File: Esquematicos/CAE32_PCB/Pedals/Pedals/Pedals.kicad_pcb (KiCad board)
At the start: 4 copper layers, 94.9 x 76.5 mm, 105 parts, among them J1 SPI_MASTER, J10 Conn_01x03_Female, J11 Conn_01x03_Female, J12 Conn_01x03_Female, J13 Conn_01x03_Female, J14 Conn_01x03_Female, J15 USB_C_Receptacle, J16 UART_PGR, J17 ST-Link, J18 LC_2, J19 LC_1, J2 CAN, J20 LC_3, J3 PGRM and SPI, J4 Conn_01x03_Female, J5 Conn_01x03_Female, J6 Conn_01x03_Female, J7 Conn_01x03_Female, J8 Conn_01x03_Female, J9 Conn_01x03_Female, Q1 MMBT3906, Q2 MMBT3906, Q3 MMBT3906, SW1 CONFIG, SW2 BOOT, SW3 RST, U1 STM32F072RBTx, U2 REF3033, U3 ADC128S102, U4 LDL1117, U5 HX711, U6 HX711, U7 HX711

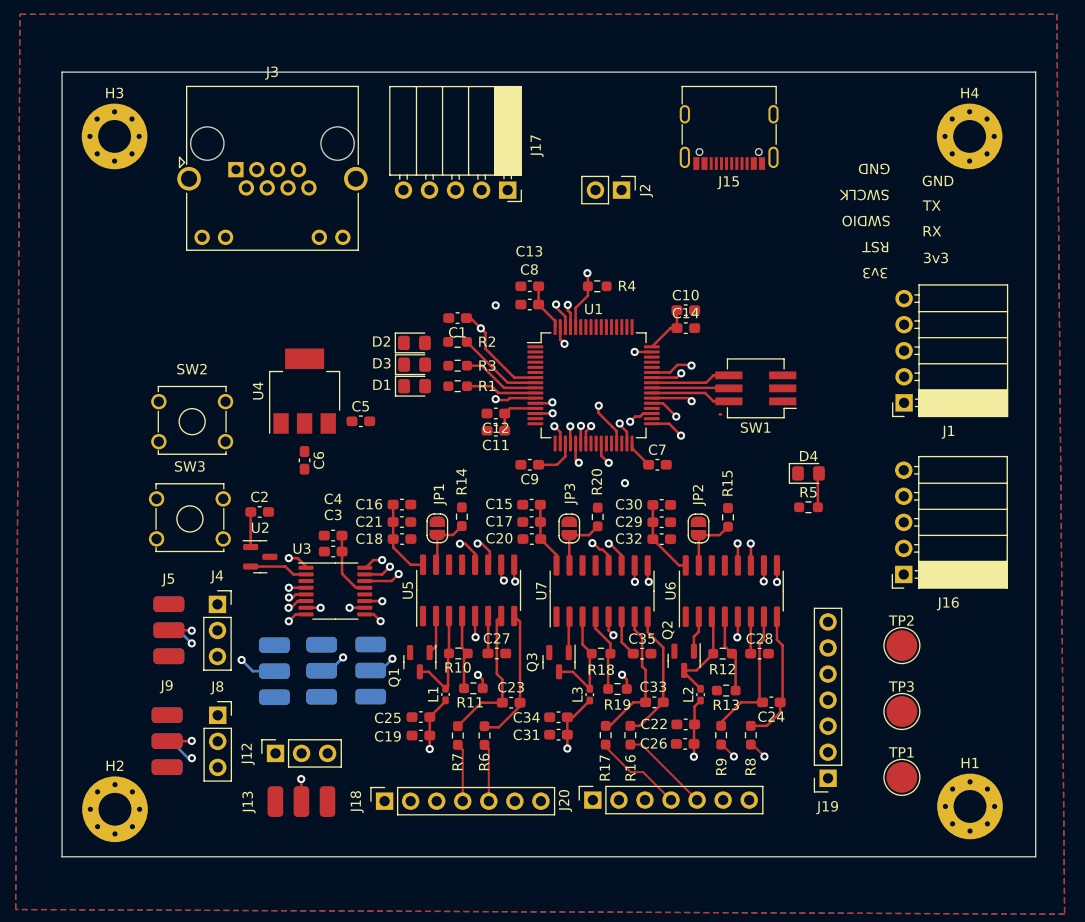
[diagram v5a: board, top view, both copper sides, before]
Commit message: Update: esquematicos de PCB, reorganizando elementos para hacer mas compacta la pcb, ademas de agregar serigrafia e imagenes de la PCB
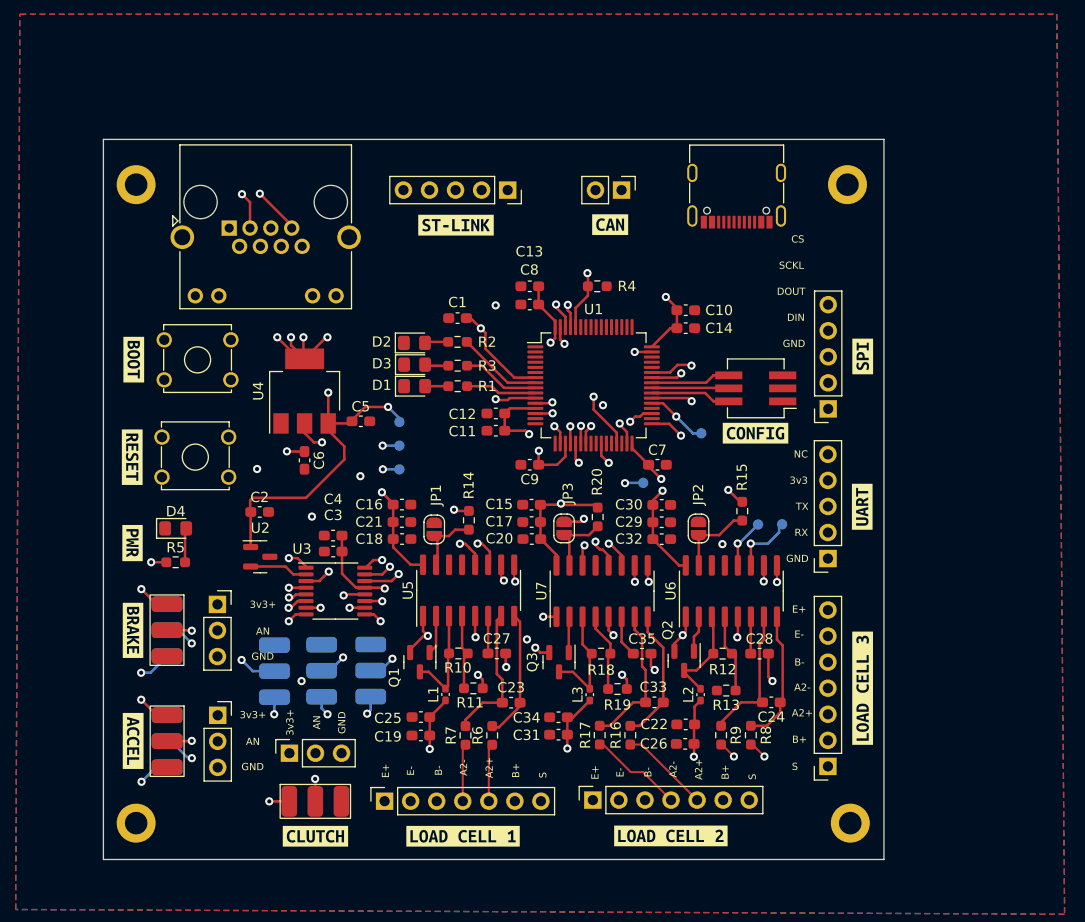
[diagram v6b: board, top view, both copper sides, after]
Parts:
- added TP4: TestPoint, TestPoint:TestPoint_Pad_D1.0mm, B.Cu at (163.8, 91.0)
- added TP5: TestPoint, TestPoint:TestPoint_Pad_D1.0mm, B.Cu at (169.3, 99.9)
- added TP6: TestPoint, TestPoint:TestPoint_Pad_D1.0mm, B.Cu at (171.7, 99.9)
- added TP7: TestPoint, TestPoint:TestPoint_Pad_D1.0mm, B.Cu at (158.1, 95.9)
- added kibuzzard-649339C9: G***, kibuzzard-649339C9, F.Cu at (140.6, 130.3)
- added kibuzzard-64933A47: G***, kibuzzard-64933A47, F.Cu at (160.8, 130.3)
- added kibuzzard-64933AAF: G***, kibuzzard-64933AAF, F.Cu at (179.5, 115.9)
- added kibuzzard-64933E22: G***, kibuzzard-64933E22, F.Cu at (126.2, 130.3)
- added kibuzzard-64934685: G***, kibuzzard-64934685, F.Cu at (108.4, 121.0)
- added kibuzzard-64934750: G***, kibuzzard-64934750, F.Cu at (108.4, 110.3)
- added kibuzzard-64934CFB: G***, kibuzzard-64934CFB, F.Cu at (108.5, 83.9)
- added kibuzzard-64934D05: G***, kibuzzard-64934D05, F.Cu at (108.3, 93.4)
- added kibuzzard-64935B19: G***, kibuzzard-64935B19, F.Cu at (169.1, 91.0)
- added kibuzzard-64935FC0: G***, kibuzzard-64935FC0, F.Cu at (179.5, 98.2)
- added kibuzzard-649360F1: G***, kibuzzard-649360F1, F.Cu at (108.4, 101.8)
- added kibuzzard-649361A8: G***, kibuzzard-649361A8, F.Cu at (179.5, 83.6)
- added kibuzzard-64936236: G***, kibuzzard-64936236, F.Cu at (154.9, 70.7)
- added kibuzzard-64936313: G***, kibuzzard-64936313, B.Cu at (111.7, 116.1)
- added kibuzzard-64936394: G***, kibuzzard-64936394, B.Cu at (111.8, 105.5)
- added kibuzzard-6493639C: G***, kibuzzard-6493639C, B.Cu at (121.3, 109.5)
- added kibuzzard-649363C1: G***, kibuzzard-649363C1, B.Cu at (126.8, 109.6)
- added kibuzzard-649363D8: G***, kibuzzard-649363D8, B.Cu at (134.9, 109.5)
- added kibuzzard-649376D0: G***, kibuzzard-649376D0, F.Cu at (139.9, 70.8)
- H1, H2, H3, H4: footprint MountingHole:MountingHole_3.2mm_M3_Pad_Via -> MountingHole:MountingHole_2.2mm_M2_DIN965_Pad
- J1, J16, J17: footprint Connector_PinSocket_2.54mm:PinSocket_1x05_P2.54mm_Horizontal -> Connector_PinSocket_2.54mm:PinSocket_1x05_P2.54mm_Vertical
- TP1, TP2, TP3: footprint TestPoint:TestPoint_Pad_D3.0mm -> TestPoint:TestPoint_Pad_D1.0mm; moved to B.Cu
- moved D4 61.9 mm to (112.6, 100.3)
- moved R5 61.9 mm to (112.6, 103.6)
- moved TP1 57.5 mm to (134.4, 94.6), turned to 180 degrees
- moved TP3 55.4 mm to (134.4, 92.3), turned to 180 degrees
- moved TP2 53.6 mm to (134.4, 89.9), turned to 180 degrees
- moved H4 12.8 mm to (178.1, 66.8)
- moved H1 11.8 mm to (178.3, 129.1)
- moved J16 7.55 mm to (176.2, 103.3)
- moved J1 7.42 mm to (176.2, 88.7)
- moved SW2 6.05 mm to (114.7, 83.9)
- moved SW3 6.05 mm to (114.5, 93.4)
- moved J15 5.76 mm to (167.2, 66.7)
- moved J3 5.74 mm to (117.8, 71.0)
- moved H3 5.15 mm to (108.7, 66.8)
- moved H2 2.46 mm to (108.7, 129.1)
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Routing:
- net +3.3V: track 50.0 -> 124.3 mm, vias 0 -> 31
- net +5V: track 3.43 -> 66.0 mm, vias 0 -> 3
- net /CS_ADC: track 38.6 -> 70.9 mm
- net /DIN: track 35.5 -> 63.3 mm, vias 2 -> 3
- net /BOOT: track 56.6 -> 81.3 mm, vias 1 -> 2
- net /ADCs components/Custom_4: track 46.0 -> 28.9 mm
- net GNDREF: track 18.6 -> 34.9 mm, vias 10 -> 23
- net /S_CKL: track 65.8 -> 55.6 mm
- net /PGR_UART_TX: track 31.2 -> 24.2 mm
- net /PGR_UART_RX: track 31.8 -> 25.3 mm
- net /NRST: track 55.9 -> 51.1 mm
- net /LOAD_CELL_CLK: track 71.0 -> 75.1 mm
- net /S_CS_PEDALS: track 56.7 -> 52.7 mm
- net /S_DOUT: track 51.3 -> 47.8 mm
- net /SCKL: track 69.8 -> 66.6 mm
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- added copper zone on In1.Cu, net +3.3V
- added copper zone on In2.Cu, net +3.3V
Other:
- board size 94.9 x 76.5 mm -> 76.1 x 70.2 mm
- board text added: "3v3+"
- board text added: "5v"
- board text added: "A2+"
- board text added: "A2-"
- board text added: "AN"
- board text added: "B+"
- board text added: "B-"
- board text added: "CS"
- board text added: "DIN"
- board text added: "DOUT"
- board text added: "E+"
- board text added: "E-"
- board text added: "LC1"
- board text added: "LC2"
- board text added: "LC3"
- board text added: "LCLK"
- board text added: "NC"
- board text added: "Pedals's version: 2.0 Revision: 1 URL: https://github.com/janc18/CAE32"
- board text added: "S"
- board text added: "SCKL"
- board text removed: "RST"
- board text removed: "SWCLK"
- board text removed: "SWDIO"

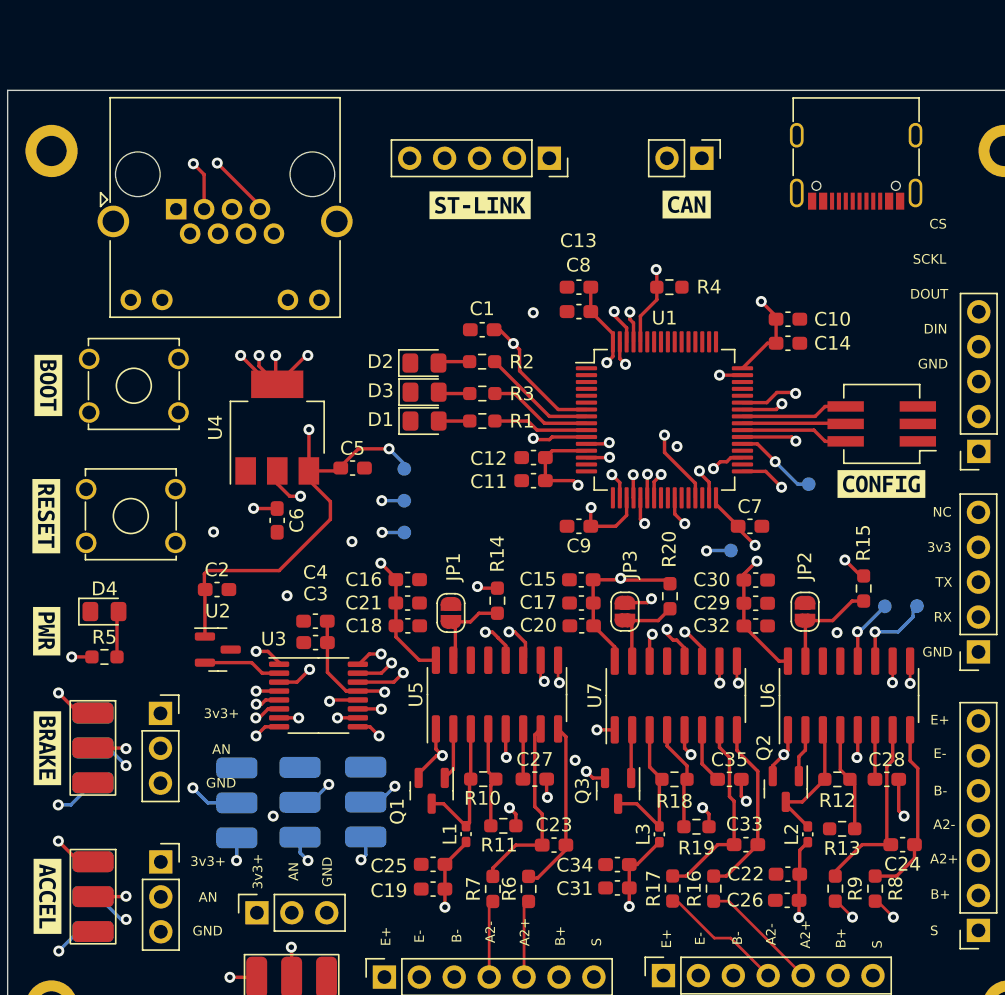
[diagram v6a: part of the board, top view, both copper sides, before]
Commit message: update: se crea la primera revisión de la PCB
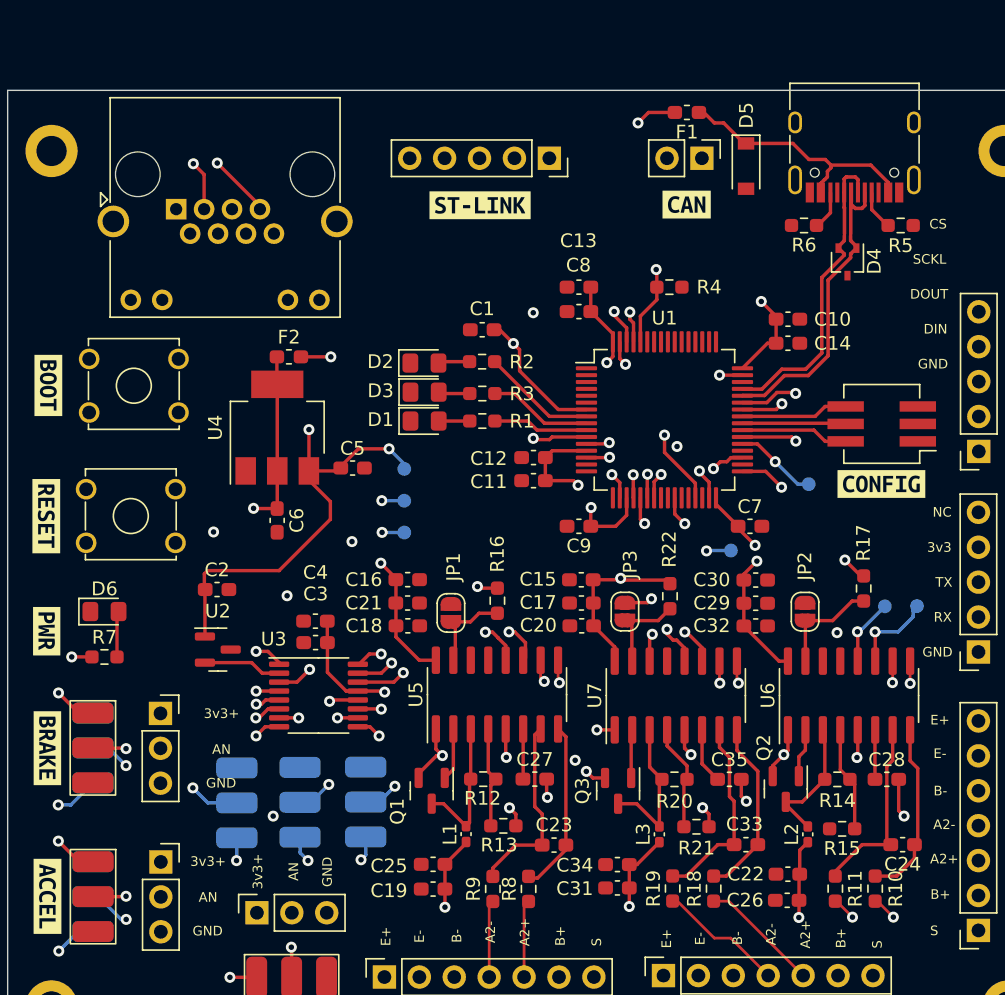
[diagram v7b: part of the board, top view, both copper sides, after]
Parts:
- added D4: VCAN26A2-03GHE3, Package_TO_SOT_SMD:SOT-323_SC-70, F.Cu at (166.6, 74.9)
- added D5: SMF5V0A, Diode_SMD:D_SOD-123, F.Cu at (159.2, 67.9)
- added F1: 0467002-NRHF, Fuse:Fuse_0603_1608Metric_Pad1.05x0.95mm_HandSolder, F.Cu at (154.9, 64.0)
- added F2: 0466-500NRHF, Fuse:Fuse_0603_1608Metric_Pad1.05x0.95mm_HandSolder, F.Cu at (126.0, 81.8)
- added R5: 5K1, Resistor_SMD:R_0603_1608Metric_Pad0.98x0.95mm_HandSolder, F.Cu at (170.5, 72.2)
- added R6: 5K1, Resistor_SMD:R_0603_1608Metric_Pad0.98x0.95mm_HandSolder, F.Cu at (163.5, 72.2)
- J15: value USB_C_Receptacle -> USB_C_Receptacle_USB2.0; footprint Connector_USB:USB_C_Receptacle_G-Switch_GT-USB-7010ASV -> Connector_USB:USB_C_Receptacle_HRO_TYPE-C-31-M-12
- moved J15 0.96 mm to (167.1, 65.8)
- renumbered D4 to D6, R8 to R10, R9 to R11, R10 to R12, R11 to R13, R12 to R14, R13 to R15, R14 to R16, R15 to R17, R16 to R18, R17 to R19, R18 to R20, R19 to R21, R20 to R22, R5 to R7, R6 to R8, R7 to R9
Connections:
- C6 pad 1: +3.3V -> Net-(C6-Pad1)
- J15 pad A5: unconnected-(J15-PadA5) -> Net-(J15-PadA5)
- J15 pad B5: unconnected-(J15-PadB5) -> Net-(J15-PadB5)
- U4 pad 2: +3.3V -> Net-(C6-Pad1)
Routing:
- net +5V: track 66.0 -> 104.9 mm, vias 3 -> 4
- net /D-: track 0.00 -> 23.3 mm
- net /D+: track 0.00 -> 22.6 mm
- net Net-(D5-Pad1): track 0.00 -> 18.6 mm
- net +3.3V: track 124.3 -> 110.4 mm, vias 31 -> 27
- net Net-(C6-Pad1): track 0.00 -> 13.5 mm
- net Net-(J15-PadA5): track 0.00 -> 2.92 mm
- net Net-(J15-PadB5): track 0.00 -> 2.87 mm

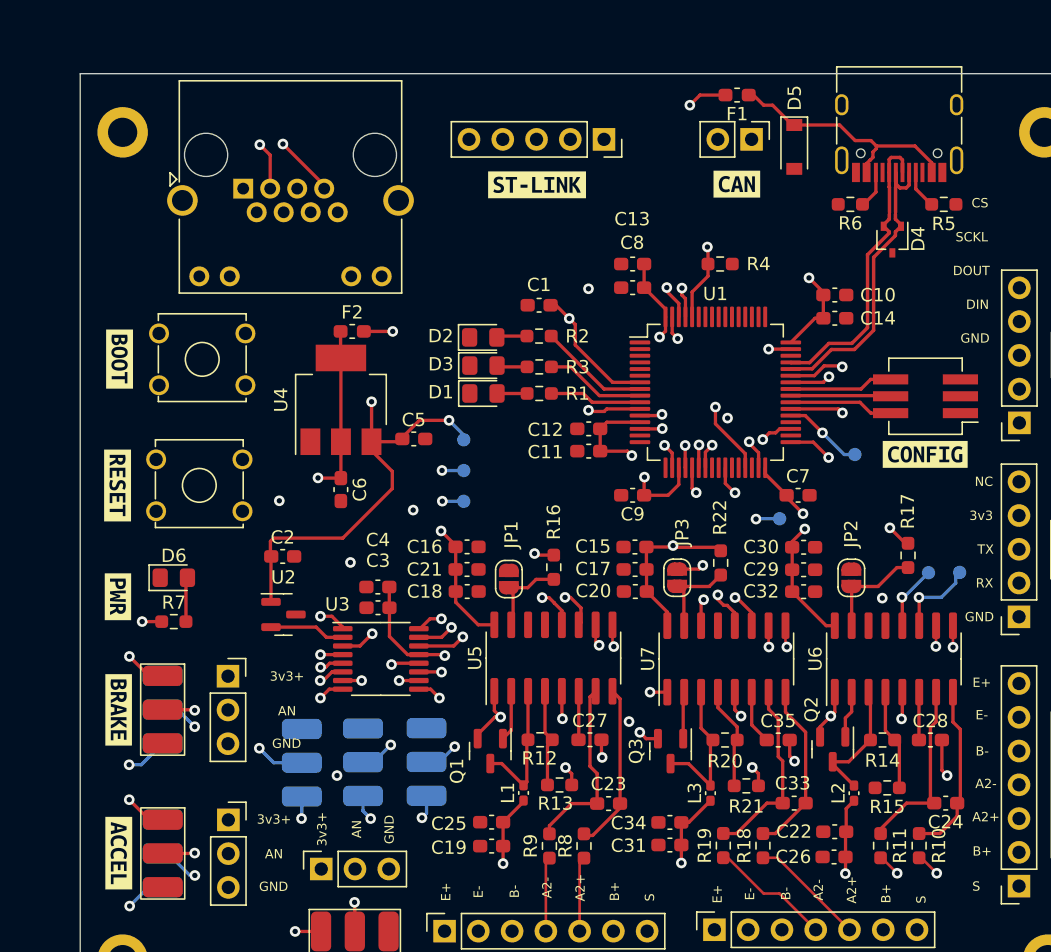
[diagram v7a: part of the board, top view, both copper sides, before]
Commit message: add: se añade un fusible extra para proteger el circuito de 5v al regulador de voltage de 3v3
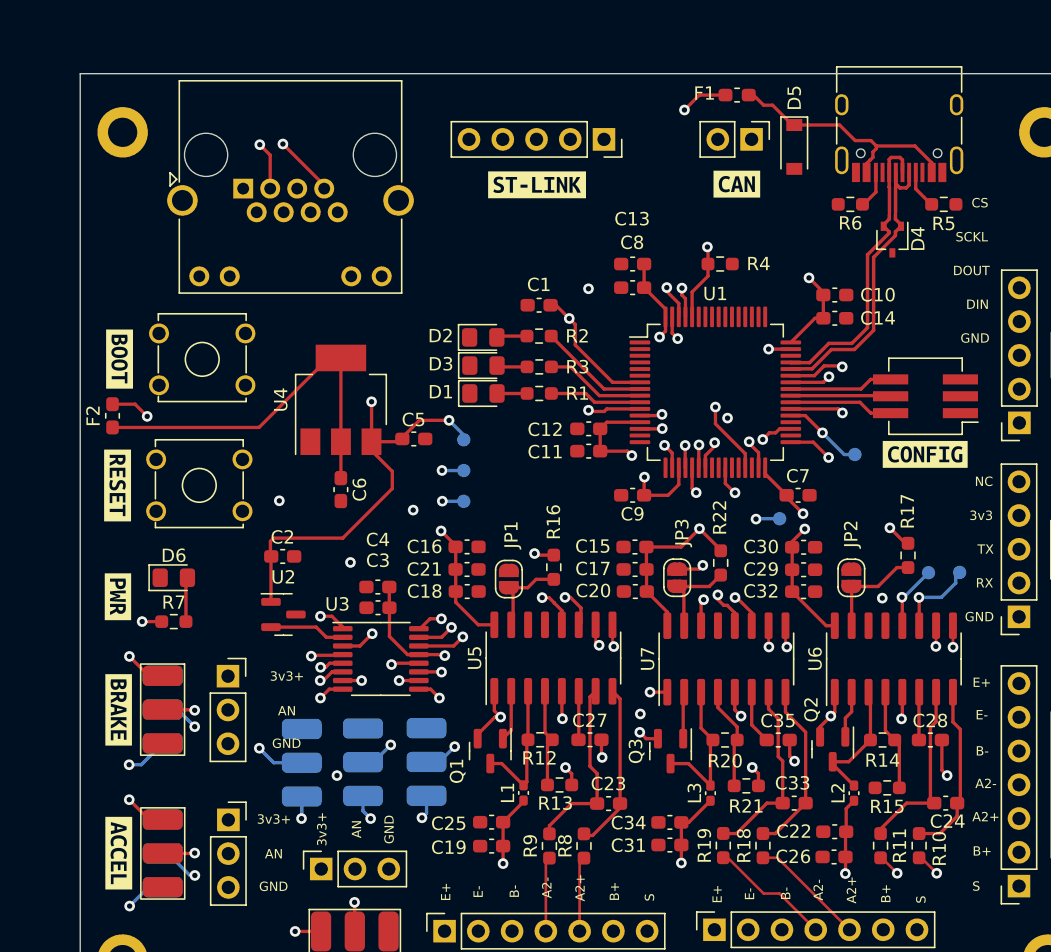
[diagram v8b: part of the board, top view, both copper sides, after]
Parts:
- moved F2 19.1 mm to (108.0, 88.1), turned to 90 degrees
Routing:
- net Net-(C6-Pad1): track 13.5 -> 27.5 mm
- net +3.3V: track 110.4 -> 112.3 mm, vias 27 -> 26
- net /D-: track 23.3 -> 22.4 mm
